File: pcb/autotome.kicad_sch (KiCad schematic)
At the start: 61 parts, among them SW1 SW_PUSH, SW10 SW_PUSH, SW11 SW_PUSH, SW12 SW_PUSH, SW13 SW_PUSH, SW14 SW_PUSH, SW15 SW_PUSH, SW16 SW_PUSH, SW17 SW_PUSH, SW18 SW_PUSH, SW19 SW_PUSH, SW2 SW_PUSH, SW20 SW_PUSH, SW21 SW_PUSH, SW22 SW_PUSH, SW23 SW_PUSH, SW24 SW_PUSH, SW25 SW_PUSH, SW26 SW_PUSH, SW27 SW_PUSH, SW28 SW_PUSH, SW3 SW_PUSH, SW4 SW_PUSH, SW5 SW_PUSH, SW6 SW_PUSH, SW7 SW_PUSH, SW8 SW_PUSH, SW9 SW_PUSH, U1 ProMicro

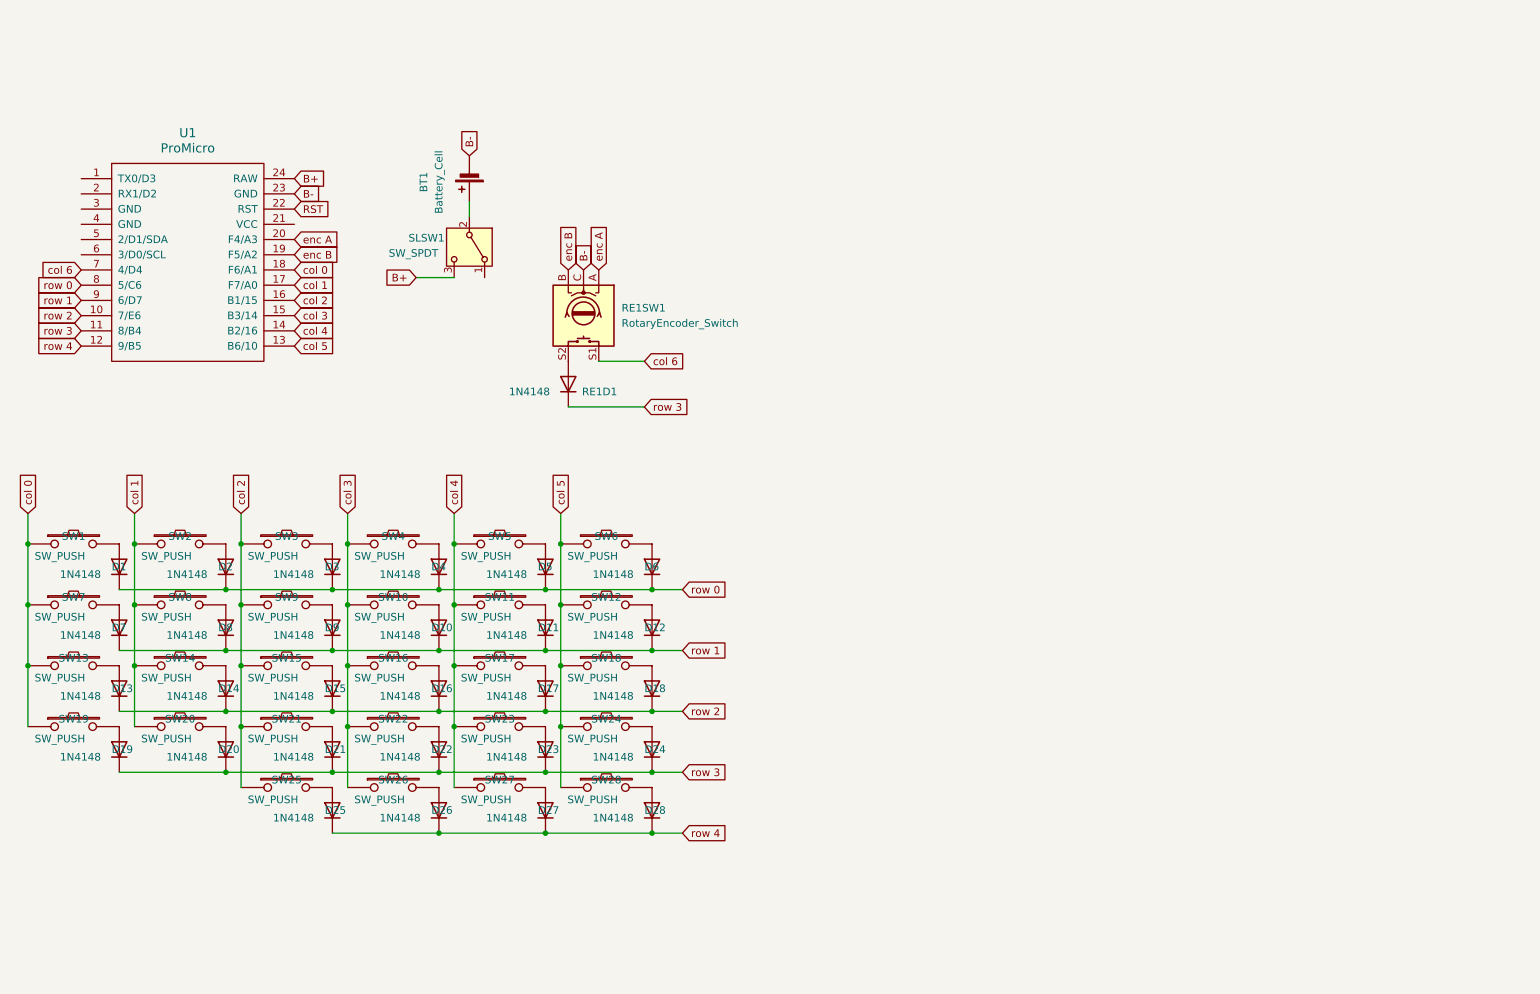
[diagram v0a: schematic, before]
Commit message: add right half to schematic
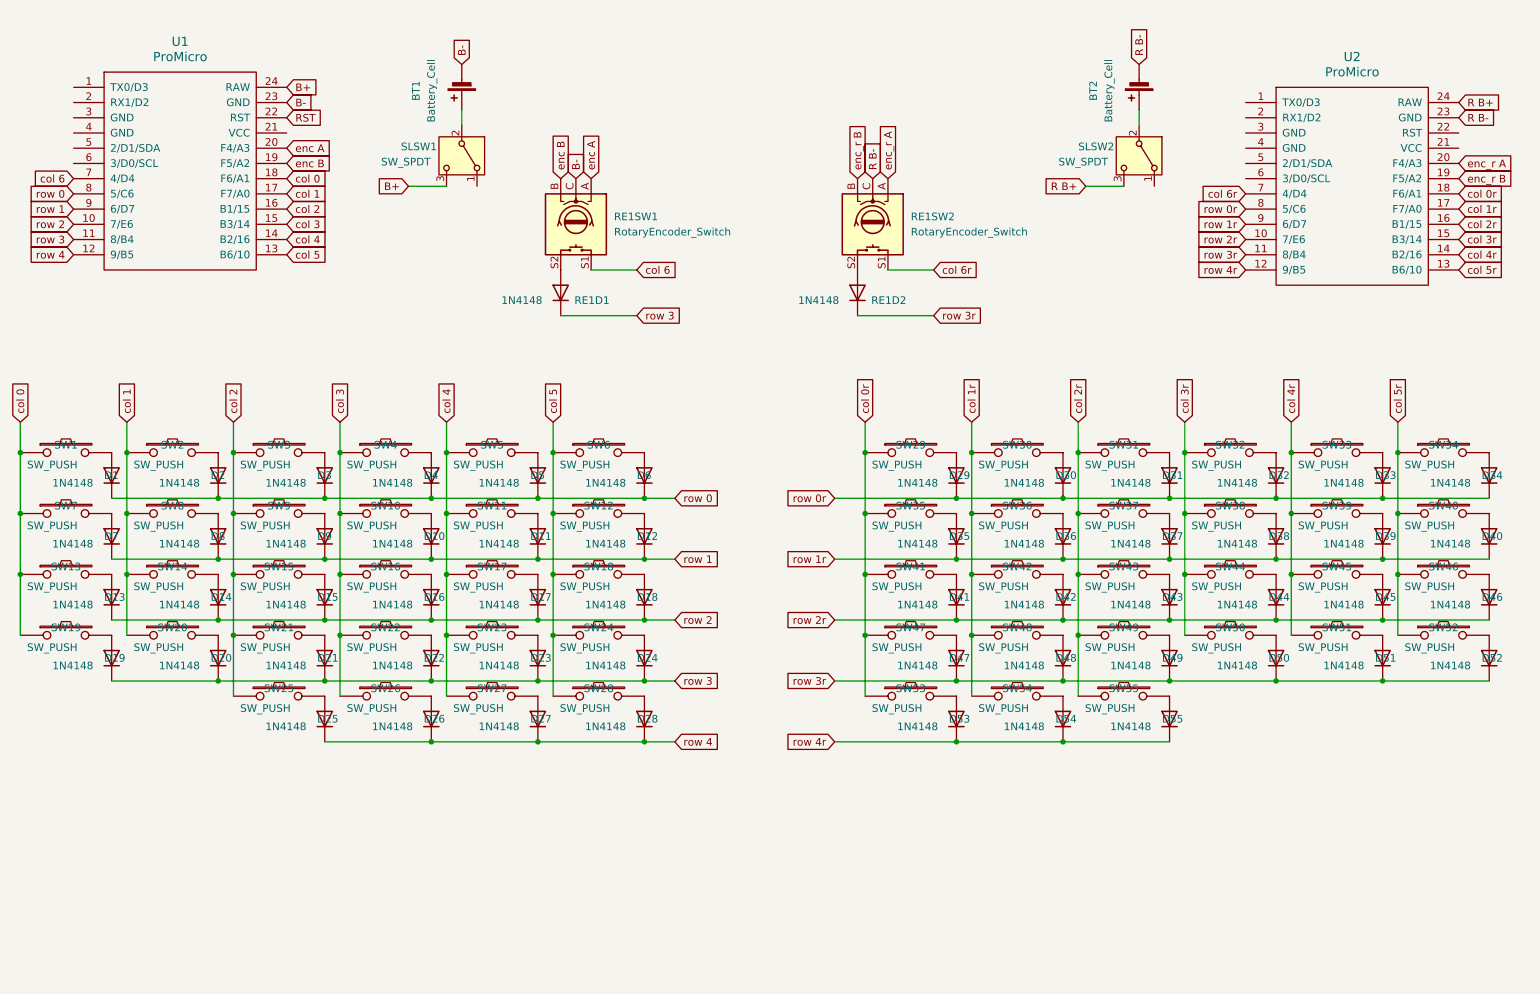
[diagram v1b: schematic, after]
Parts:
- added BT2: Battery_Cell, Connector_JST:JST_XH_B2B-XH-A_1x02_P2.50mm_Vertical, symbol Device:Battery_Cell
- added D29, D30, D31, D32, D33, D34, D35, D36, D37, D38, D39, D40, D41, D42, D43, D44, D45, D46, D47, D48, D49, D50, D51, D52, D53, D54, D55, RE1D2: 1N4148, Diode_THT:D_DO-35_SOD27_P7.62mm_Horizontal, symbol Diode:1N4148
- added RE1SW2: RotaryEncoder_Switch, autotome_library:RotaryEncoder_Alps_EC11E-Switch_Vertical_H20mm, symbol Device:RotaryEncoder_Switch
- added SLSW2: SW_SPDT, Button_Switch_THT:SW_Slide_SPDT_Straight_CK_OS102011MS2Q, symbol Switch:SW_SPDT
- added SW29, SW30, SW31, SW32, SW33, SW34, SW35, SW36, SW37, SW38, SW39, SW40, SW41, SW42, SW43, SW44, SW45, SW46, SW47, SW48, SW49, SW50, SW51, SW52, SW53, SW54, SW55: SW_PUSH, PCM_Switch_Keyboard_Hotswap_Kailh:SW_Hotswap_Kailh_MX_Plated_1.00u, symbol kbd:SW_PUSH
- added U2: ProMicro, autotome_library:NiceNano, symbol kbd:ProMicro
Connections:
- new net: D36.2 (A), SW36.2
- new net: D35.2 (A), SW35.2
- new net: D38.2 (A), SW38.2
- new net: D46.2 (A), SW46.2
- new net: D39.2 (A), SW39.2
- new net: BT2.1 (+), SLSW2.2 (B)
- new net: D50.2 (A), SW50.2
- new net: D29.2 (A), SW29.2
- new net: D51.2 (A), SW51.2
- new net: D43.2 (A), SW43.2
- new net: D48.2 (A), SW48.2
- new net: D45.2 (A), SW45.2
- new net: D54.2 (A), SW54.2
- new net: D32.2 (A), SW32.2
- new net: D30.2 (A), SW30.2
- new net: D55.2 (A), SW55.2
- new net: D47.2 (A), SW47.2
- new net: D37.2 (A), SW37.2
- new net: D49.2 (A), SW49.2
- new net: D52.2 (A), SW52.2
- new net: D40.2 (A), SW40.2
- new net: D34.2 (A), SW34.2
- new net: D33.2 (A), SW33.2
- new net: D42.2 (A), SW42.2
- new net: RE1D2.2 (A), RE1SW2.S2
- new net: D31.2 (A), SW31.2
- new net: D53.2 (A), SW53.2
- new net: D41.2 (A), SW41.2
- new net: D44.2 (A), SW44.2
- new net R B+: SLSW2.3 (C), U2.24 (RAW)
- new net R B-: BT2.2 (-), RE1SW2.C, U2.23 (GND)
- new net col 0r: SW29.1, SW35.1, SW41.1, SW47.1, SW53.1, U2.18 (F6/A1)
- new net col 1r: SW30.1, SW36.1, SW42.1, SW48.1, SW54.1, U2.17 (F7/A0)
- new net col 2r: SW31.1, SW37.1, SW43.1, SW49.1, SW55.1, U2.16 (B1/15)
- new net col 3r: SW32.1, SW38.1, SW44.1, SW50.1, U2.15 (B3/14)
- new net col 4r: SW33.1, SW39.1, SW45.1, SW51.1, U2.14 (B2/16)
- new net col 5r: SW34.1, SW40.1, SW46.1, SW52.1, U2.13 (B6/10)
- new net col 6r: RE1SW2.S1, U2.7 (4/D4)
- new net enc_r A: RE1SW2.A, U2.20 (F4/A3)
- new net enc_r B: RE1SW2.B, U2.19 (F5/A2)
- new net row 0r: D29.1 (K), D30.1 (K), D31.1 (K), D32.1 (K), D33.1 (K), D34.1 (K), U2.8 (5/C6)
- new net row 1r: D35.1 (K), D36.1 (K), D37.1 (K), D38.1 (K), D39.1 (K), D40.1 (K), U2.9 (6/D7)
- new net row 2r: D41.1 (K), D42.1 (K), D43.1 (K), D44.1 (K), D45.1 (K), D46.1 (K), U2.10 (7/E6)
- new net row 3r: D47.1 (K), D48.1 (K), D49.1 (K), D50.1 (K), D51.1 (K), D52.1 (K), RE1D2.1 (K), U2.11 (8/B4)
- new net row 4r: D53.1 (K), D54.1 (K), D55.1 (K), U2.12 (9/B5)
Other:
- moved on the sheet: BT1, D1, D10, D11, D12, D13, D14, D15, D16, D17, D18, D19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

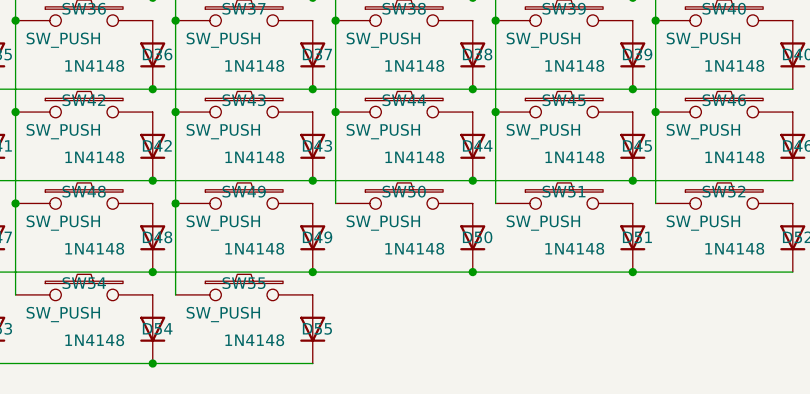
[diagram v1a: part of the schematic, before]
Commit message: add missing keyswitch
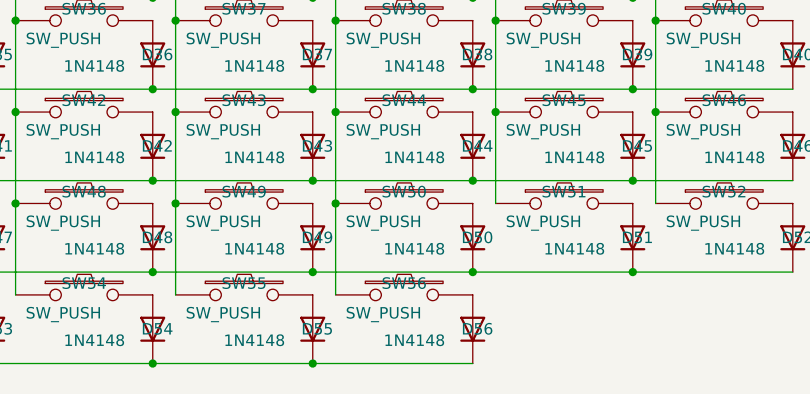
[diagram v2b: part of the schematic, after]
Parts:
- added D56: 1N4148, Diode_THT:D_DO-35_SOD27_P7.62mm_Horizontal, symbol Diode:1N4148
- added SW56: SW_PUSH, PCM_Switch_Keyboard_Hotswap_Kailh:SW_Hotswap_Kailh_MX_Plated_1.00u, symbol kbd:SW_PUSH
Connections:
- net col 3r: now also SW56.1
- net row 4r: now also D56.1 (K)
- new net: D56.2 (A), SW56.2
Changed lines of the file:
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@@
 	)
 	(junction
+		(at 217.17 125.73)
+		(diameter 0)
+		(color 0 0 0 0)
+	)
+	(junction
 		(at 76.2 125.73)
 		(diameter 0)
@@
 	)
 	(junction
+		(at 214.63 143.51)
+		(diameter 0)
+		(color 0 0 0 0)
+	)
+	(junction
 		(at 214.63 113.03)
 		(diameter 0)
@@
 	(wire
 		(pts
+			(xy 214.63 143.51) (xy 232.41 143.51)
+		)
+		(stroke
+			(width 0)
+			(type default)
+		)
+	)
+	(wire
+		(pts
 			(xy 199.39 95.25) (xy 199.39 105.41)
 		)
@@
 	(wire
 		(pts
+			(xy 217.17 125.73) (xy 217.17 135.89)
+		)
+		(stroke
+			(width 0)
+			(type default)
+		)
+	)
+	(wire
+		(pts
 			(xy 73.66 113.03) (xy 91.44 113.03)
 		)
@@
 	(symbol
 		(lib_id "Diode:1N4148")
+		(at 232.41 139.7 90)
+		(unit 1)
+		(body_style 1)
+		(exclude_from_sim no)
+		(in_bom yes)
+		(on_board yes)
+		(in_pos_files yes)
+		(dnp no)
+		(property "Reference" "D56"
+			(at 231.14 139.7 90)
+			(show_name no)
+			(do_not_autoplace no)
+			(effects
+				(font
+					(size 1.27 1.27)
+				)
+				(justify right)
+			)
+		)
+		(property "Value" "1N4148"
+			(at 222.504 140.97 90)
+			(show_name no)
+			(do_not_autoplace no)
+			(effects
+				(font
+					(size 1.27 1.27)
+				)
+				(justify right)
+			)
+		)
+		(property "Footprint" "Diode_THT:D_DO-35_SOD27_P7.62mm_Horizontal"
+			(at 232.41 139.7 0)
+			(hide yes)
+			(show_name no)
+			(do_not_autoplace no)
+			(effects
+				(font
+					(size 1.27 1.27)
+				)
+			)
+		)
+		(property "Datasheet" "https://assets.nexperia.com/documents/data-sheet/1N4148_1N4448.pdf"
+			(at 232.41 139.7 0)
+			(hide yes)
+			(show_name no)
+			(do_not_autoplace no)
+			(effects
+				(font
+					(size 1.27 1.27)
+				)
+			)
+		)
+		(property "Description" "100V 0.15A standard switching diode, DO-35"
+			(at 232.41 139.7 0)
+			(hide yes)
+			(show_name no)
+			(do_not_autoplace no)
+			(effects
+				(font
+					(size 1.27 1.27)
+				)
+			)
+		)
+		(property "Sim.Device" "D"
+			(at 232.41 139.7 0)
+			(hide yes)
+			(show_name no)
+			(do_not_autoplace no)
+			(effects
+				(font
+					(size 1.27 1.27)
+				)
+			)
+		)
+		(property "Sim.Pins" "1=K 2=A"
+			(at 232.41 139.7 0)
+			(hide yes)
+			(show_name no)
+			(do_not_autoplace no)
+			(effects
+				(font
+					(size 1.27 1.27)
+				)
+			)
+		)
+		(pin "1"
+		)
+		(pin "2"
+		)
+		(instances
+			(project "autotome"
+				(path "/7a8f7727-35b5-4a31-8719-22ef542e3f8e"
+					(reference "D56")
+					(unit 1)
+				)
+			)
+		)
+	)
+	(symbol
+		(lib_id "Diode:1N4148")
 		(at 73.66 129.54 90)
 		(unit 1)
@@
 					(unit 1)
 				)
+			)
+		)
+	)
+	(symbol
+		(lib_id "kbd:SW_PUSH")
+		(at 224.79 135.89 0)
+		(unit 1)
+		(body_style 1)
+		(exclude_from_sim no)
+		(in_bom yes)
+		(on_board yes)
+		(in_pos_files yes)
+		(dnp no)
+		(property "Reference" "SW56"
+			(at 224.79 134.62 0)
+			(show_name no)
+			(do_not_autoplace no)
+			(effects
+				(font
+					(size 1.27 1.27)
+				)
+			)
+		)
+		(property "Value" "SW_PUSH"
+			(at 222.504 137.922 0)
+			(show_name no)
+			(do_not_autoplace no)
+			(effects
+				(font
+					(size 1.27 1.27)
+				)
+			)
+		)
+		(property "Footprint" "PCM_Switch_Keyboard_Hotswap_Kailh:SW_Hotswap_Kailh_MX_Plated_1.00u"
+			(at 224.79 135.89 0)
+			(hide yes)
+			(show_name no)
+			(do_not_autoplace no)
+			(effects
+				(font
+					(size 1.27 1.27)
+				)
+			)
+		)
+		(property "Datasheet" ""
+			(at 224.79 135.89 0)
+			(show_name no)
+			(do_not_autoplace no)
+			(effects
+				(font
+					(size 1.27 1.27)
+				)
+			)
+		)
+		(property "Description" ""
+			(at 224.79 135.89 0)
+			(hide yes)
+			(show_name no)
+			(do_not_autoplace no)
+			(effects
+				(font
+					(size 1.27 1.27)
+				)
+			)
+		)
+		(pin "1"
+		)
+		(pin "2"
+		)
+		(instances
+			(project "autotome"
+				(path "/7a8f7727-35b5-4a31-8719-22ef542e3f8e"
+					(reference "SW56")
+					(unit 1)
+				)

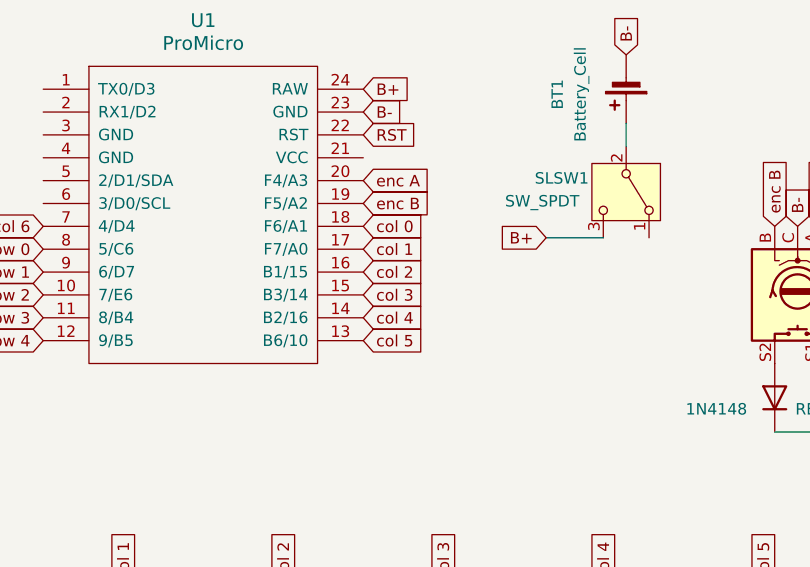
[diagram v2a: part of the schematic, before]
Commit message: reverse order of columns in left half
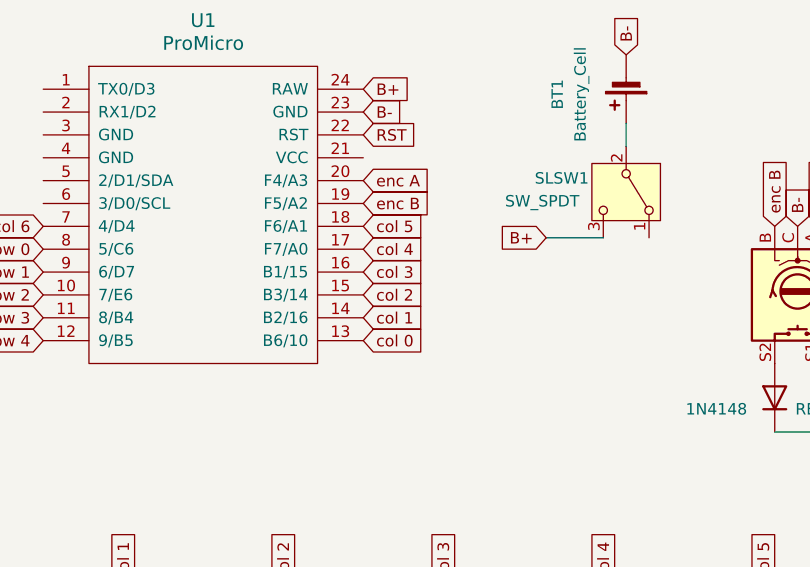
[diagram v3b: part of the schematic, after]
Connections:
- net col 0: now also U1.13 (B6/10); no longer U1.18 (F6/A1)
- net col 1: now also U1.14 (B2/16); no longer U1.17 (F7/A0)
- net col 2: now also U1.15 (B3/14); no longer U1.16 (B1/15)
- net col 3: now also U1.16 (B1/15); no longer U1.15 (B3/14)
- net col 4: now also U1.17 (F7/A0); no longer U1.14 (B2/16)
- net col 5: now also U1.18 (F6/A1); no longer U1.13 (B6/10)

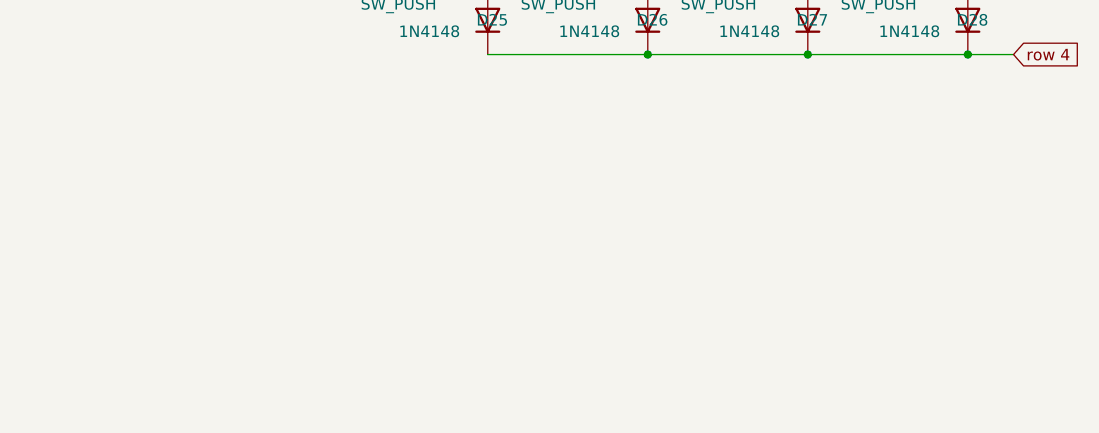
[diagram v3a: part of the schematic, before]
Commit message: add pads on left half for reconnecting breakaway
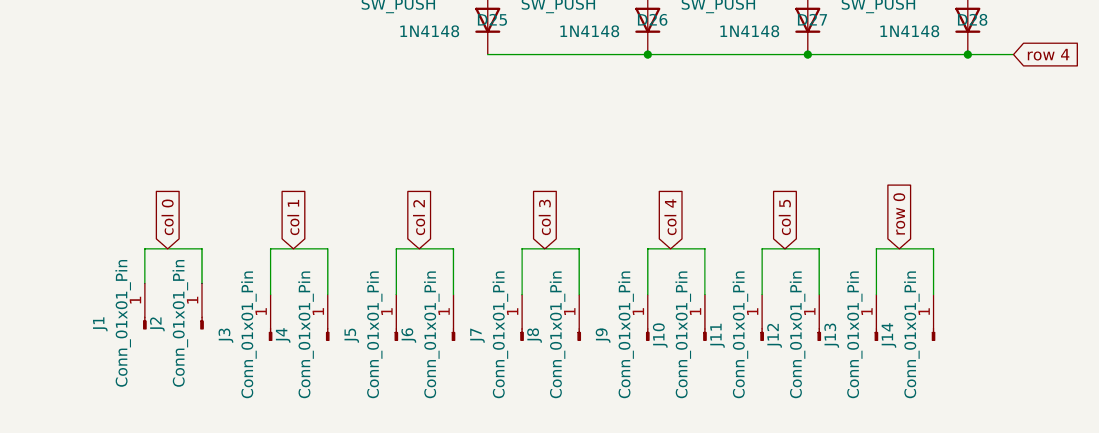
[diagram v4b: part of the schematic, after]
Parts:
- added J1, J10, J11, J12, J13, J14, J2, J3, J4, J5, J6, J7, J8, J9: Conn_01x01_Pin, TestPoint:TestPoint_THTPad_1.0x1.0mm_Drill0.5mm, symbol Connector:Conn_01x01_Pin
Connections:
- net col 0: now also J1.1 (Pin_1), J2.1 (Pin_1)
- net col 1: now also J3.1 (Pin_1), J4.1 (Pin_1)
- net col 2: now also J5.1 (Pin_1), J6.1 (Pin_1)
- net col 3: now also J7.1 (Pin_1), J8.1 (Pin_1)
- net col 4: now also J10.1 (Pin_1), J9.1 (Pin_1)
- net col 5: now also J11.1 (Pin_1), J12.1 (Pin_1)
- net row 0: now also J13.1 (Pin_1), J14.1 (Pin_1)

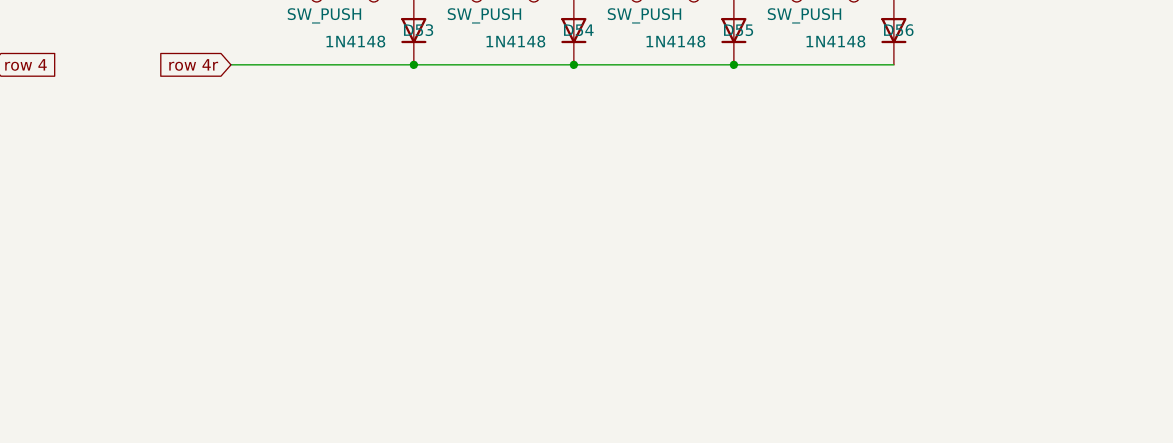
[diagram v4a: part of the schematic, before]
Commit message: add pads on right half for reconnecting breakaway
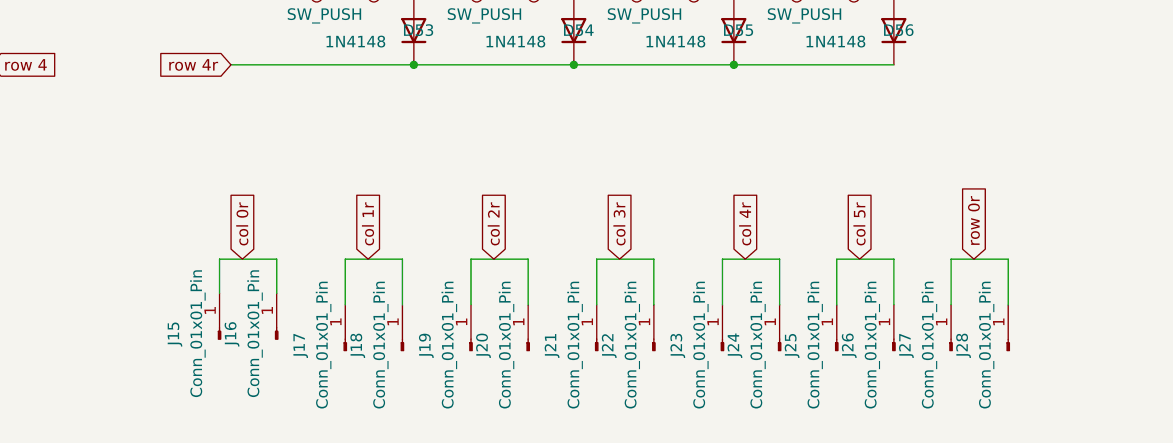
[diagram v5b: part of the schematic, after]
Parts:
- added J15, J16, J17, J18, J19, J20, J21, J22, J23, J24, J25, J26, J27, J28: Conn_01x01_Pin, TestPoint:TestPoint_THTPad_1.0x1.0mm_Drill0.5mm, symbol Connector:Conn_01x01_Pin
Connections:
- net col 0r: now also J15.1 (Pin_1), J16.1 (Pin_1)
- net col 1r: now also J17.1 (Pin_1), J18.1 (Pin_1)
- net col 2r: now also J19.1 (Pin_1), J20.1 (Pin_1)
- net col 3r: now also J21.1 (Pin_1), J22.1 (Pin_1)
- net col 4r: now also J23.1 (Pin_1), J24.1 (Pin_1)
- net col 5r: now also J25.1 (Pin_1), J26.1 (Pin_1)
- net row 0r: now also J27.1 (Pin_1), J28.1 (Pin_1)
